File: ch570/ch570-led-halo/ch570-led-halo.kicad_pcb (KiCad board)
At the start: 2 copper layers, 42 x 26.8 mm, 53 parts, among them J1 SAO, J2 USB_C_Receptacle_USB2.0_16P, SW2 TS-1187A-B-A-B, U1 CH572D, U2 AW32001, U3 QMC6309, U4 USBLC6-2SC6, U7 MG6229D4-28, Y1 32MHz

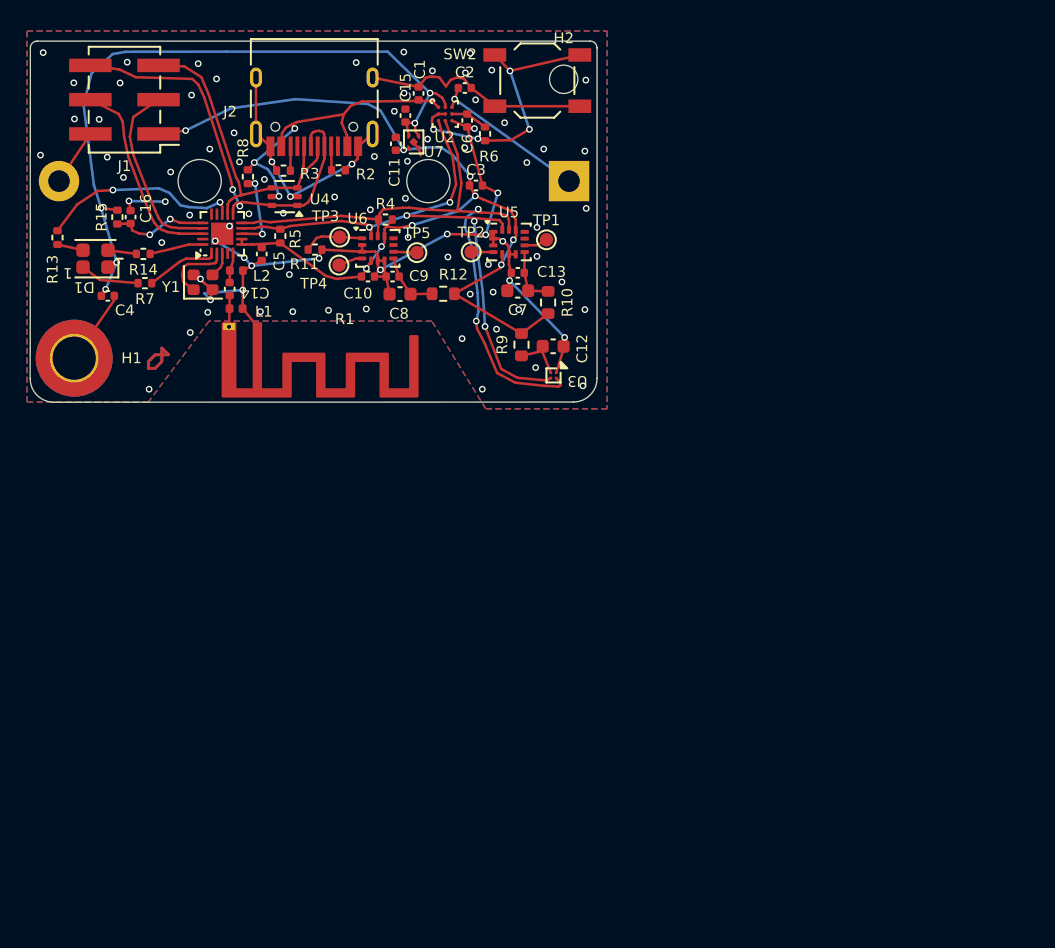
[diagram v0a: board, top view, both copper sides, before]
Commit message: Update design with new ch570 board
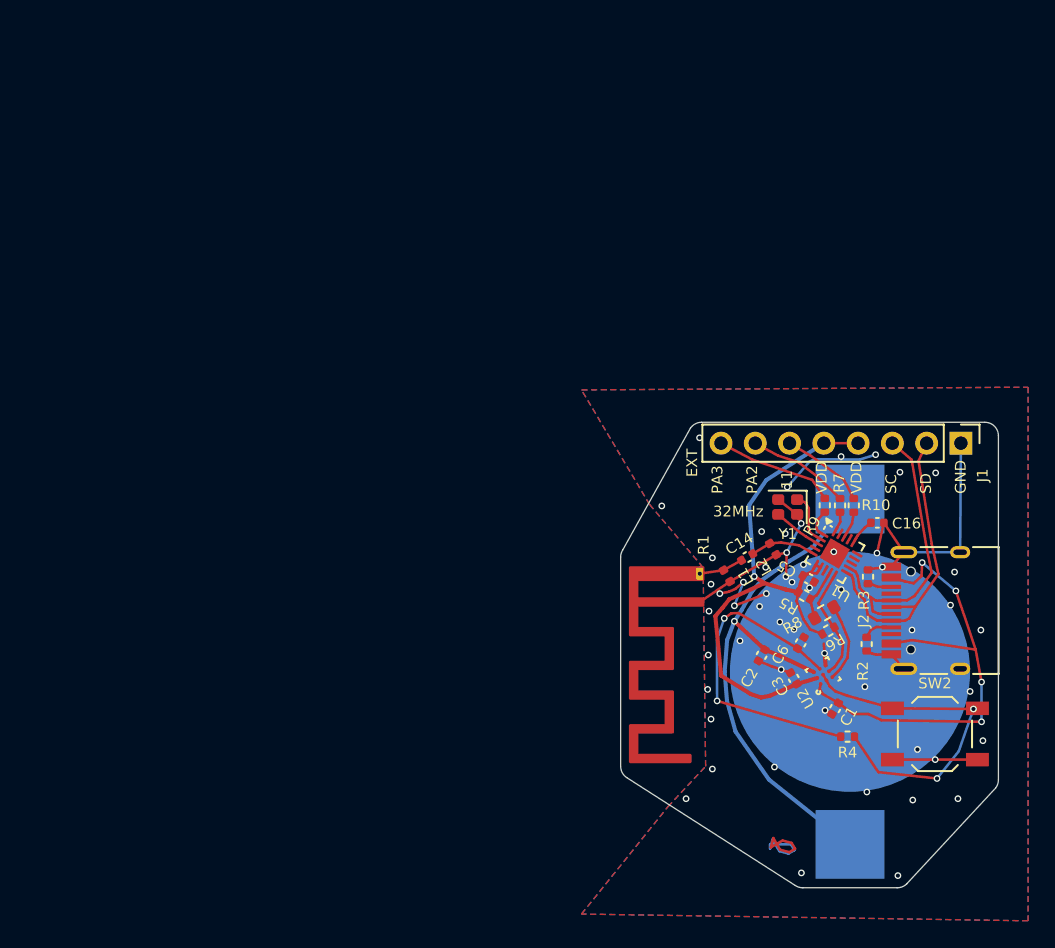
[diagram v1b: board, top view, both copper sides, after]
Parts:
- removed C10, C11, C13, C9: 0.1μF, Capacitor_SMD:C_0402_1005Metric
- removed C12, C7, C8: 22μF, Capacitor_SMD:C_0603_1608Metric
- removed C15: 1u, Capacitor_SMD:C_0402_1005Metric
- removed C4: 0.1u, Capacitor_SMD:C_0402_1005Metric
- removed D1: A-SP1923XR6GHB1C-M01-3T, LED_SMD:LED_RGB_Wuerth_150080M153000
- removed H1: HOLE, MountingHole:MountingHole_3.2mm_M3_ISO7380_Pad_TopBottom
- removed H2: BATTMOUNT, MountingHole:MountingHole_2.1mm
- removed R11, R15: 5.1k, Resistor_SMD:R_0402_1005Metric
- removed R12: 33Ω, Resistor_SMD:R_0603_1608Metric
- removed R13, R14: 1k, Resistor_SMD:R_0402_1005Metric
- removed TP1: INT2, TestPoint:TestPoint_Pad_D1.0mm
- removed TP2, TP4, TP5: INT1, TestPoint:TestPoint_Pad_D1.0mm
- removed TP3: SA0, TestPoint:TestPoint_Pad_D1.0mm
- removed U3: QMC6309, Package_BGA:WLP-4_0.83x0.83mm_P0.4mm
- removed U4: USBLC6-2SC6, Package_TO_SOT_SMD:SOT-363_SC-70-6
- removed U5, U6: ~, cnhardware:LGA-14_3x2.5mm_P0.5mm_LayoutBorder3x4y_EVEN_PADS
- removed U7: MG6229D4-28, cnhardware:xdfn-reg
- BT1: footprint Battery:BatteryHolder_Bulgin_BX0123_1xCR123 -> Battery:BatteryHolder_Keystone_3002_1x2032
- J1: value SAO -> EXT; footprint Connector_PinHeader_2.54mm:PinHeader_2x03_P2.54mm_Vertical_SMD -> Connector_PinHeader_2.54mm:PinHeader_1x08_P2.54mm_Vertical
- R10, R9: value 33Ω -> 10; footprint Resistor_SMD:R_0603_1608Metric -> Resistor_SMD:R_0402_1005Metric
- R7: value 1k -> 10
- R8: value NP -> 0; footprint Resistor_SMD:R_0402_1005Metric -> Resistor_SMD:R_0603_1608Metric
- moved J1 67.0 mm to (132.7, 64.0), turned to -90 degrees
- moved J2 60.6 mm to (131.6, 76.5), turned to 90 degrees
- moved C16 59.8 mm to (126.5, 70.0), turned to 0 degrees
- moved SW2 56.7 mm to (130.8, 85.6)
- moved C1 55.1 mm to (123.4, 83.7), turned to -120 degrees
- moved R7 54.1 mm to (123.8, 68.7), turned to -90 degrees
- moved R8 53.6 mm to (122.6, 76.6), turned to -150 degrees
- moved R3 52.8 mm to (125.8, 74.0), turned to 90 degrees
- moved R2 52.6 mm to (125.7, 78.9), turned to -90 degrees
- moved R4 51.4 mm to (124.3, 85.8), turned to 180 degrees
- moved U1 51.2 mm to (123.4, 72.2), turned to -30 degrees
- moved U2 50.1 mm to (122.5, 81.2), turned to 120 degrees
- moved C2 47.5 mm to (118.0, 79.8), turned to -120 degrees
- moved C5 47.1 mm to (121.4, 74.1), turned to -30 degrees
- moved R5 47.1 mm to (121.1, 75.3), turned to 150 degrees
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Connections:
- net LED renamed VMEASURE
- J1 pad 1: VDD -> GND
- J1 pad 2: GND -> SWD
- J1 pad 3: PA10 -> SWCLK
- J1 pad 4: PA11 -> VDD
- J1 pad 5: SWCLK -> VDD
- J1 pad 6: SWD -> Net-(J1-Pin_6)
- R10 pad 1: Net-(U5-VDD) -> Net-(J1-Pin_6)
- R10 pad 2: VDD -> PA11
- R4 pad 1: SCL -> PWRINT
- R4 pad 2: VDD -> Net-(U2-VDD)
- R6 pad 1: PWRINT -> VDD
- R6 pad 2: Net-(U2-VDD) -> SCL
- R7 pad 1: PA3 -> Net-(J1-Pin_7)
- R7 pad 2: Net-(D1-RK) -> PA2
- R8 pad 1: Net-(U1-V5) -> Net-(U2-SDA)
- R8 pad 2: +5V -> SDA
- R9 pad 1: Net-(U3-VDD) -> Net-(J1-Pin_8)
- R9 pad 2: VDD -> PA3
- U1 pad 13: PA4 -> unconnected-(U1-PA4/SCS/PWM4/TMR2-Pad13)
- U1 pad 17: PA10 -> unconnected-(U1-PA10/R6/T7-Pad17)
- U1 pad 8: Net-(U1-V5) -> unconnected-(U1-V5-Pad8)
- U2 pad A2: Net-(D1-A) -> VDD
- U2 pad C1: SDA -> Net-(U2-SDA)
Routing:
- net Net-(D1-A): track 52.7 -> 0.00 mm, vias 5 -> 0
- net SDA: track 46.3 -> 3.92 mm, vias 5 -> 0
- net SCL: track 48.5 -> 8.30 mm, vias 2 -> 0
- net VDD: track 72.5 -> 43.9 mm, vias 9 -> 1
- net +BATT: track 11.9 -> 40.2 mm
- net Net-(U2-VDD): track 2.76 -> 24.3 mm, vias 0 -> 2
- net PA4: track 14.8 -> 0.00 mm, vias 2 -> 0
- net PA10: track 13.7 -> 0.00 mm
- net PA11: track 14.7 -> 1.96 mm
- net +5V: track 24.8 -> 36.0 mm, vias 3 -> 4
- net (no net): track 0.00 -> 10.4 mm
- net SWD: track 31.8 -> 22.6 mm, vias 2 -> 0
- net Net-(J1-Pin_8): track 0.00 -> 8.96 mm
- net Net-(J1-Pin_7): track 0.00 -> 7.61 mm
- net Net-(J1-Pin_6): track 0.00 -> 6.43 mm
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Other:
- board size 42 x 26.8 mm -> 28 x 34.5 mm
- board text added: "PA3 PA2 11 SWC SWD GND"
- board text added: "PA3 PA2 11 VDD VDD SC SD GND"
- board text added: "ch570-led-halo rev-"
- board text removed: "ch570cr123 - revA"

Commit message: Update designs
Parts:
- added C15: 1u, Capacitor_SMD:C_0402_1005Metric, F.Cu at (119.9, 81.5)
- added R11: 0, Resistor_SMD:R_0402_1005Metric, F.Cu at (118.5, 76.5)
- added U4: MG6229D4-28, cnhardware:xdfn-reg, F.Cu at (118.1, 75.2)
- moved C3 6.95 mm to (119.6, 74.6), turned to 90 degrees
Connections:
- J1 pad 4: VDD -> Net-(J1-Pin_4)
- J1 pad 5: VDD -> Net-(J1-Pin_4)
- U1 pad 17: unconnected-(U1-PA10/R6/T7-Pad17) -> GND
- U1 pad 4: unconnected-(U1-NC-Pad4) -> GND
- U2 pad A2: VDD -> Net-(J1-Pin_4)
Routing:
- net VDD: track 43.9 -> 11.5 mm, vias 1 -> 0
- net Net-(J1-Pin_4): track 0.00 -> 31.3 mm, vias 0 -> 1
- net GND: track 114.6 -> 137.4 mm, vias 54 -> 55
- net PWRINT: track 25.4 -> 24.8 mm

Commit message: Bump all designs per order
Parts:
- added U3: RCLAMP0502N, cnhardware:DFN-6_1.2x1.0mm_P0.4mm, F.Cu at (129.8, 69.2)
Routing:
- net +5V: track 36.3 -> 43.0 mm
- net GND: track 137.4 -> 138.2 mm, vias 55 -> 56
